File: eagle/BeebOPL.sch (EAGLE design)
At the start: 43 parts, among them IC1 LM324N, IC2 YM3014B, IC3 7805TV, IC5 74LS02N, IC6 YM3812, IC7 74LS04N, IC9 74HCT688N, J1 1 MHz Bus, J2 Feed-through, J3 3.5mm Jack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

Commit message: Added power options
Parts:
- removed S3: LED, SparkFun-Retired:JUMPER-2PTH
- added JP2, JP3, JP4: (no value), pinhead:PINHD-1X2/90
- added U$1: IRFD9024DIL, YMSynth:IRFD9024DIL
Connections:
- removed net N$28: C6.-, C7.2
- removed net N$29: C6.+, C7.1
- net GND: now also C6.-, C7.2, JP2.2, JP3.2, JP4.2, U$1.G; no longer S3.1
- net N$17: now also JP3.1
- net N$25: now also JP4.1; no longer S3.2
- net VCC: now also C6.+, C7.1, JP2.1, U$1.D, U$1.S
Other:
- note added: "Divide track to use power MOSFET"
- moved on the sheet: C6, C7, J4
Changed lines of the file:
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@@
 <part name="P+2" library="supply1" deviceset="VCC" device=""/>
 <part name="GND3" library="supply1" deviceset="GND" device=""/>
-<part name="S3" library="SparkFun-Retired" deviceset="JUMPER-2" device="PTH" value="LED"/>
 <part name="LED1" library="led" deviceset="LED" device="5MM"/>
 <part name="R9" library="resistor" deviceset="R-EU_" device="0207/10" value="470R"/>
@@
 <part name="P+12" library="supply1" deviceset="VCC" device=""/>
 <part name="GND13" library="supply1" deviceset="GND" device=""/>
+<part name="U$1" library="YMSynth" deviceset="IRFD9024" device="DIL"/>
+<part name="GND18" library="supply1" deviceset="GND" device=""/>
+<part name="JP2" library="pinhead" deviceset="PINHD-1X2" device="/90"/>
+<part name="GND19" library="supply1" deviceset="GND" device=""/>
+<part name="P+7" library="supply1" deviceset="VCC" device=""/>
+<part name="GND20" library="supply1" deviceset="GND" device=""/>
+<part name="JP3" library="pinhead" deviceset="PINHD-1X2" device="/90"/>
+<part name="GND21" library="supply1" deviceset="GND" device=""/>
+<part name="JP4" library="pinhead" deviceset="PINHD-1X2" device="/90"/>
 </parts>
 <sheets>
@@
 addresses &amp;FC04
 and &amp;FC05)</text>
-<text x="-276.86" y="0" size="1.778" layer="97">Power Jack
+<text x="-302.26" y="-12.7" size="1.778" layer="97">Power Jack
 (2.1mm centre
 positive)</text>
@@
 <text x="-273.05" y="45.72" size="1.778" layer="97">Divide track to use
 power regulator</text>
+<text x="-283.21" y="-11.43" size="1.778" layer="97">Divide track to use
+power MOSFET</text>
 </plain>
 <instances>
@@
 <instance part="P+6" gate="VCC" x="-182.88" y="20.32"/>
 <instance part="GND12" gate="1" x="-182.88" y="-5.08"/>
-<instance part="J4" gate="G$1" x="-266.7" y="15.24"/>
+<instance part="J4" gate="G$1" x="-292.1" y="2.54"/>
 <instance part="P+1" gate="VCC" x="91.44" y="5.08"/>
 <instance part="S1" gate="A" x="172.72" y="-63.5" rot="R90"/>
 <instance part="S2" gate="A" x="172.72" y="-50.8" rot="R90"/>
-<instance part="C7" gate="G$1" x="-165.1" y="58.42"/>
-<instance part="C6" gate="G$1" x="-154.94" y="58.42" smashed="yes">
-<attribute name="NAME" x="-153.797" y="58.9026" size="1.778" layer="95"/>
-<attribute name="VALUE" x="-153.797" y="53.8226" size="1.778" layer="96"/>
+<instance part="C7" gate="G$1" x="-250.19" y="6.35"/>
+<instance part="C6" gate="G$1" x="-240.03" y="6.35" smashed="yes">
+<attribute name="NAME" x="-238.887" y="6.8326" size="1.778" layer="95"/>
+<attribute name="VALUE" x="-238.887" y="1.7526" size="1.778" layer="96"/>
 </instance>
 <instance part="IC7" gate="A" x="-114.3" y="-10.16"/>
@@
 <instance part="P+2" gate="VCC" x="127" y="81.28"/>
 <instance part="GND3" gate="1" x="127" y="20.32"/>
-<instance part="S3" gate="A" x="-114.3" y="33.02" rot="R90"/>
 <instance part="LED1" gate="G$1" x="-127" y="35.56"/>
 <instance part="R9" gate="G$1" x="-127" y="45.72" rot="R90"/>
@@
 </instance>
 <instance part="P+12" gate="VCC" x="-274.32" y="34.29"/>
-<instance part="GND13" gate="1" x="-264.16" y="12.7"/>
+<instance part="GND13" gate="1" x="-289.56" y="0"/>
+<instance part="U$1" gate="G$1" x="-276.86" y="7.62" smashed="yes" rot="MR90">
+<attribute name="NAME" x="-274.32" y="12.7" size="1.778" layer="95" rot="MR90"/>
+<attribute name="VALUE" x="-276.86" y="12.7" size="1.778" layer="96" rot="MR90"/>
+</instance>
+<instance part="GND18" gate="1" x="-274.32" y="0"/>
+<instance part="JP2" gate="G$1" x="-297.18" y="22.86"/>
+<instance part="GND19" gate="1" x="-292.1" y="20.32"/>
+<instance part="P+7" gate="VCC" x="-245.11" y="11.43"/>
+<instance part="GND20" gate="1" x="-245.11" y="-1.27"/>
+<instance part="JP3" gate="G$1" x="184.15" y="-100.33"/>
+<instance part="GND21" gate="1" x="175.26" y="-106.68"/>
+<instance part="JP4" gate="G$1" x="-113.03" y="33.02"/>
 </instances>
 <busses>
@@
 <pinref part="LED1" gate="G$1" pin="C"/>
 <wire x1="-127" y1="27.94" x2="-127" y2="29.21" width="0.1524" layer="91"/>
-<pinref part="S3" gate="A" pin="1"/>
 <wire x1="-127" y1="29.21" x2="-127" y2="30.48" width="0.1524" layer="91"/>
-<wire x1="-111.76" y1="33.02" x2="-111.76" y2="29.21" width="0.1524" layer="91"/>
-<wire x1="-111.76" y1="29.21" x2="-127" y2="29.21" width="0.1524" layer="91"/>
+<wire x1="-120.65" y1="29.21" x2="-127" y2="29.21" width="0.1524" layer="91"/>
 <junction x="-127" y="29.21"/>
-</segment>
-<segment>
+<pinref part="JP4" gate="G$1" pin="2"/>
+<wire x1="-115.57" y1="33.02" x2="-120.65" y2="33.02" width="0.1524" layer="91"/>
+<wire x1="-120.65" y1="33.02" x2="-120.65" y2="29.21" width="0.1524" layer="91"/>
+</segment>
+<segment>
+<pinref part="GND17" gate="1" pin="GND"/>
 <pinref part="IC3" gate="A1" pin="GND"/>
-<pinref part="GND17" gate="1" pin="GND"/>
 <wire x1="-243.84" y1="24.13" x2="-243.84" y2="21.59" width="0.1524" layer="91"/>
 </segment>
 <segment>
 <pinref part="J4" gate="G$1" pin="GND"/>
-<wire x1="-264.16" y1="17.78" x2="-264.16" y2="15.24" width="0.1524" layer="91"/>
+<wire x1="-289.56" y1="5.08" x2="-289.56" y2="2.54" width="0.1524" layer="91"/>
 <pinref part="GND13" gate="1" pin="GND"/>
+</segment>
+<segment>
+<pinref part="U$1" gate="G$1" pin="G"/>
+<pinref part="GND18" gate="1" pin="GND"/>
+</segment>
+<segment>
+<pinref part="JP2" gate="G$1" pin="2"/>
+<wire x1="-299.72" y1="22.86" x2="-292.1" y2="22.86" width="0.1524" layer="91"/>
+<pinref part="GND19" gate="1" pin="GND"/>
+</segment>
+<segment>
+<pinref part="C6" gate="G$1" pin="-"/>
+<wire x1="-250.19" y1="1.27" x2="-245.11" y2="1.27" width="0.1524" layer="91"/>
+<pinref part="C7" gate="G$1" pin="2"/>
+<pinref part="GND20" gate="1" pin="GND"/>
+<wire x1="-245.11" y1="1.27" x2="-240.03" y2="1.27" width="0.1524" layer="91"/>
+<junction x="-245.11" y="1.27"/>
+</segment>
+<segment>
+<pinref part="JP3" gate="G$1" pin="2"/>
+<wire x1="181.61" y1="-100.33" x2="175.26" y2="-100.33" width="0.1524" layer="91"/>
+<wire x1="175.26" y1="-100.33" x2="175.26" y2="-104.14" width="0.1524" layer="91"/>
+<pinref part="GND21" gate="1" pin="GND"/>
 </segment>
 </net>
@@
 <wire x1="-266.7" y1="31.75" x2="-264.16" y2="31.75" width="0.1524" layer="91"/>
 <junction x="-266.7" y="31.75"/>
+<pinref part="U$1" gate="G$1" pin="S"/>
+<wire x1="-271.78" y1="10.16" x2="-266.7" y2="10.16" width="0.1524" layer="91"/>
+<wire x1="-266.7" y1="10.16" x2="-266.7" y2="31.75" width="0.1524" layer="91"/>
 <pinref part="J4" gate="G$1" pin="PWR"/>
-<wire x1="-264.16" y1="22.86" x2="-264.16" y2="31.75" width="0.1524" layer="91"/>
-<junction x="-264.16" y="31.75"/>
+<pinref part="U$1" gate="G$1" pin="D"/>
+<wire x1="-289.56" y1="10.16" x2="-284.48" y2="10.16" width="0.1524" layer="91"/>
+<wire x1="-284.48" y1="10.16" x2="-281.94" y2="10.16" width="0.1524" layer="91"/>
+<wire x1="-284.48" y1="10.16" x2="-284.48" y2="-3.81" width="0.1524" layer="91"/>
+<wire x1="-284.48" y1="-3.81" x2="-266.7" y2="-3.81" width="0.1524" layer="91"/>
+<wire x1="-266.7" y1="-3.81" x2="-266.7" y2="10.16" width="0.1524" layer="91"/>
+<junction x="-266.7" y="10.16"/>
+<pinref part="JP2" gate="G$1" pin="1"/>
+<wire x1="-299.72" y1="25.4" x2="-284.48" y2="25.4" width="0.1524" layer="91"/>
+<wire x1="-284.48" y1="25.4" x2="-284.48" y2="10.16" width="0.1524" layer="91"/>
+<junction x="-284.48" y="10.16"/>
+</segment>
+<segment>
+<pinref part="C7" gate="G$1" pin="1"/>
+<wire x1="-250.19" y1="8.89" x2="-245.11" y2="8.89" width="0.1524" layer="91"/>
+<pinref part="C6" gate="G$1" pin="+"/>
+<pinref part="P+7" gate="VCC" pin="VCC"/>
+<wire x1="-245.11" y1="8.89" x2="-240.03" y2="8.89" width="0.1524" layer="91"/>
+<junction x="-245.11" y="8.89"/>
 </segment>
 </net>
@@
 <wire x1="175.26" y1="-63.5" x2="175.26" y2="-73.66" width="0.1524" layer="91"/>
 <junction x="175.26" y="-73.66"/>
+<wire x1="175.26" y1="-73.66" x2="175.26" y2="-97.79" width="0.1524" layer="91"/>
+<pinref part="JP3" gate="G$1" pin="1"/>
+<wire x1="175.26" y1="-97.79" x2="181.61" y2="-97.79" width="0.1524" layer="91"/>
 </segment>
 </net>
@@
 <wire x1="-127" y1="38.1" x2="-127" y2="39.37" width="0.1524" layer="91"/>
 <wire x1="-127" y1="39.37" x2="-127" y2="40.64" width="0.1524" layer="91"/>
-<wire x1="-127" y1="39.37" x2="-111.76" y2="39.37" width="0.1524" layer="91"/>
+<wire x1="-127" y1="39.37" x2="-120.65" y2="39.37" width="0.1524" layer="91"/>
 <junction x="-127" y="39.37"/>
-<pinref part="S3" gate="A" pin="2"/>
-<wire x1="-111.76" y1="39.37" x2="-111.76" y2="35.56" width="0.1524" layer="91"/>
+<pinref part="JP4" gate="G$1" pin="1"/>
+<wire x1="-115.57" y1="35.56" x2="-120.65" y2="35.56" width="0.1524" layer="91"/>
+<wire x1="-120.65" y1="35.56" x2="-120.65" y2="39.37" width="0.1524" layer="91"/>
 </segment>
 </net>
@@
 </segment>
 </net>
-<net name="N$29" class="1">
-<segment>
-<pinref part="C7" gate="G$1" pin="1"/>
-<wire x1="-165.1" y1="60.96" x2="-154.94" y2="60.96" width="0.1524" layer="91"/>
-<pinref part="C6" gate="G$1" pin="+"/>
-</segment>
-</net>
-<net name="N$28" class="3">
-<segment>
-<wire x1="-167.64" y1="53.34" x2="-165.1" y2="53.34" width="0.1524" layer="91"/>
-<pinref part="C6" gate="G$1" pin="-"/>
-<wire x1="-165.1" y1="53.34" x2="-154.94" y2="53.34" width="0.1524" layer="91"/>
-<pinref part="C7" gate="G$1" pin="2"/>
-<junction x="-165.1" y="53.34"/>
-</segment>
-</net>

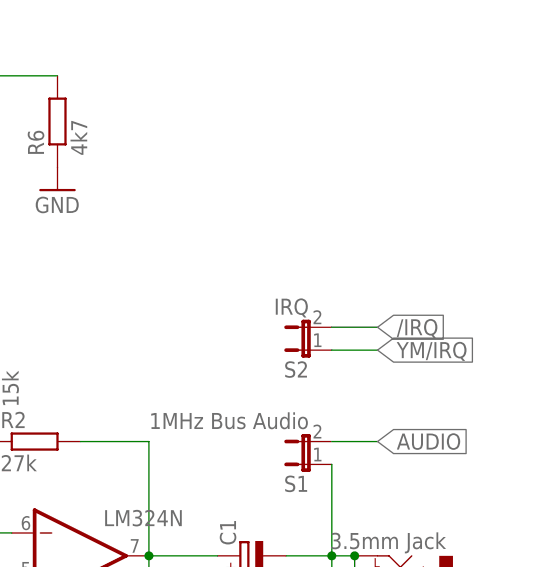
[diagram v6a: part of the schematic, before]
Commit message: Set IRQ as connected by default
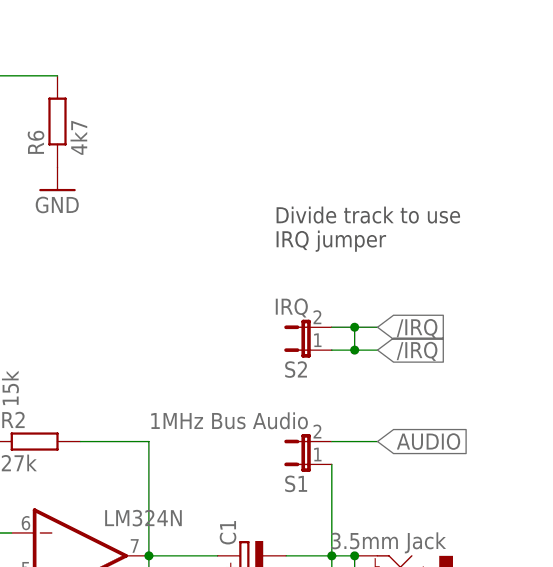
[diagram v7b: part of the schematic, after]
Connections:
- net /IRQ: now also S2.1
- net YM/IRQ: no longer S2.1
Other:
- note added: "Divide track to use IRQ jumper"
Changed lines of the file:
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@@
 <setting verticaltext="up"/>
 </settings>
-<grid distance="0.05" unitdist="inch" unit="inch" style="lines" multiple="1" display="no" altdistance="0.01" altunitdist="inch" altunit="inch"/>
+<grid distance="0.1" unitdist="inch" unit="inch" style="lines" multiple="1" display="no" altdistance="0.01" altunitdist="inch" altunit="inch"/>
 <layers>
 <layer number="1" name="Top" color="4" fill="1" visible="no" active="no"/>
@@
 <text x="-283.21" y="-11.43" size="1.778" layer="97">Divide track to use
 power MOSFET</text>
+<text x="168.91" y="-39.37" size="1.778" layer="97">Divide track to use
+IRQ jumper</text>
 </plain>
 <instances>
@@
 </segment>
 <segment>
+<pinref part="S2" gate="A" pin="1"/>
+<wire x1="175.26" y1="-50.8" x2="177.8" y2="-50.8" width="0.1524" layer="91"/>
+<label x="180.34" y="-50.8" size="1.778" layer="95" xref="yes"/>
 <pinref part="S2" gate="A" pin="2"/>
-<wire x1="175.26" y1="-48.26" x2="180.34" y2="-48.26" width="0.1524" layer="91"/>
+<wire x1="177.8" y1="-50.8" x2="180.34" y2="-50.8" width="0.1524" layer="91"/>
+<wire x1="175.26" y1="-48.26" x2="177.8" y2="-48.26" width="0.1524" layer="91"/>
 <label x="180.34" y="-48.26" size="1.778" layer="95" xref="yes"/>
+<wire x1="177.8" y1="-48.26" x2="180.34" y2="-48.26" width="0.1524" layer="91"/>
+<wire x1="177.8" y1="-50.8" x2="177.8" y2="-48.26" width="0.1524" layer="91"/>
+<junction x="177.8" y="-50.8"/>
+<junction x="177.8" y="-48.26"/>
 </segment>
 </net>
@@
 <label x="15.24" y="40.64" size="1.778" layer="95" xref="yes"/>
 </segment>
-<segment>
-<pinref part="S2" gate="A" pin="1"/>
-<wire x1="175.26" y1="-50.8" x2="180.34" y2="-50.8" width="0.1524" layer="91"/>
-<label x="180.34" y="-50.8" size="1.778" layer="95" xref="yes"/>
-</segment>
-</net>
+</net>

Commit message: Tidied-up schematic
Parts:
- removed JP1: JUMPER-3PTH, SparkFun-Retired:JUMPER-3PTH
- removed JP2: (no value), pinhead:PINHD-1X2/90
- removed U$1: IRFD9024DIL, YMSynth:IRFD9024DIL
- added JP5: (no value), pinhead:PINHD-1X4/90
- added S3: JUMPER-3PTH, SparkFun-Retired:JUMPER-3PTH
- added TR1: IRFD9024DIL, YMSynth:IRFD9024DIL
- IC3: value 7805TV -> LM7805
- RN1, RN2, RN3, RN4: value 2K2 -> 2k2
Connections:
- removed net YM/IRQ: IC6./IRQ
- net /IRQ: now also IC6./IRQ
- net GND: now also JP5.2, JP5.3, TR1.G; no longer JP2.2, U$1.G
- net N$27: now also S3.3; no longer JP1.3
- net VCC: now also JP5.4, S3.1, S3.2, TR1.D, TR1.S; no longer JP1.1, JP1.2, JP2.1, U$1.D, U$1.S
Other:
- note added: "Bob's board (text behind YM3812)"
- note added: "Check whether I want to change the footprint of the 3.5mm connector"
- note added: "DATE: 29 Sept 2016"
- note added: "IMPORTANT – Check board for links at: 3 pin jumper MOSFET IRQ jumper"
- note added: "Make sure signals pass through links correctly"
- note added: "Need to change the mount holes to 4mm diam (but expressed in inches) to fit common stand-offs"
- note added: "To do"
- note removed: "DATE: 27 Sept 2016"
- note removed: "Designed by: Robert Lazarus (with assistance from David Banks & Mark) Based on the Commodore Sound Expander (Richard Watts & Music Sales Limited, 1985)"
- moved on the sheet: C5, C6, C7, C9, H1, H2, H3, H4, IC3, IC5A, IC5B, IC5C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
